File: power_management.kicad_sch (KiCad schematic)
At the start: 36 parts, among them U1 TPS65185

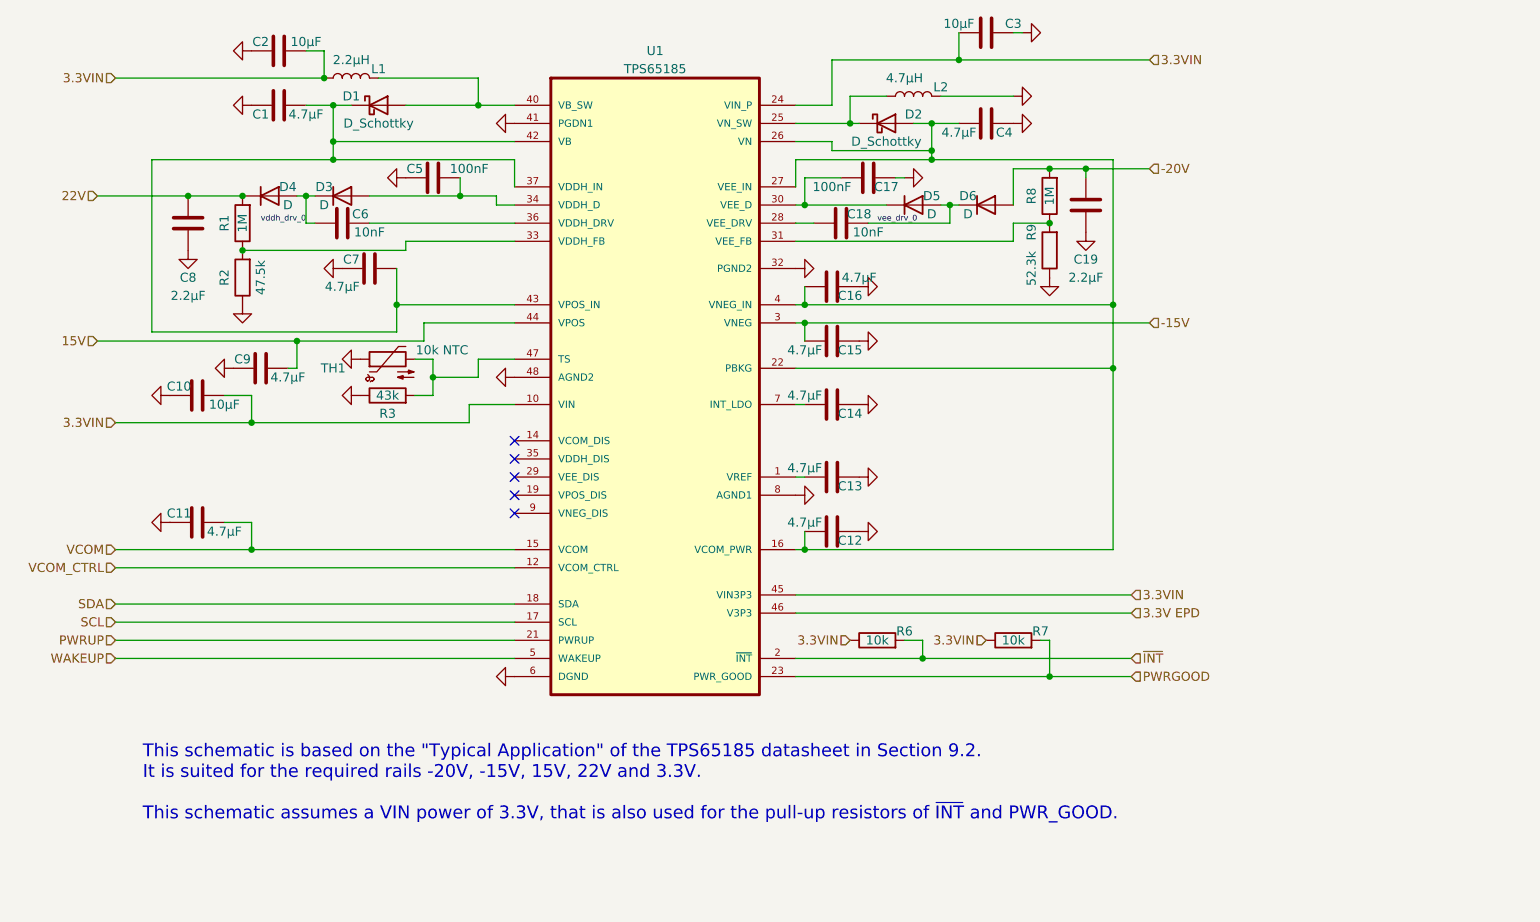
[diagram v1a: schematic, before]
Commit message: Set voltage rating of capacitors
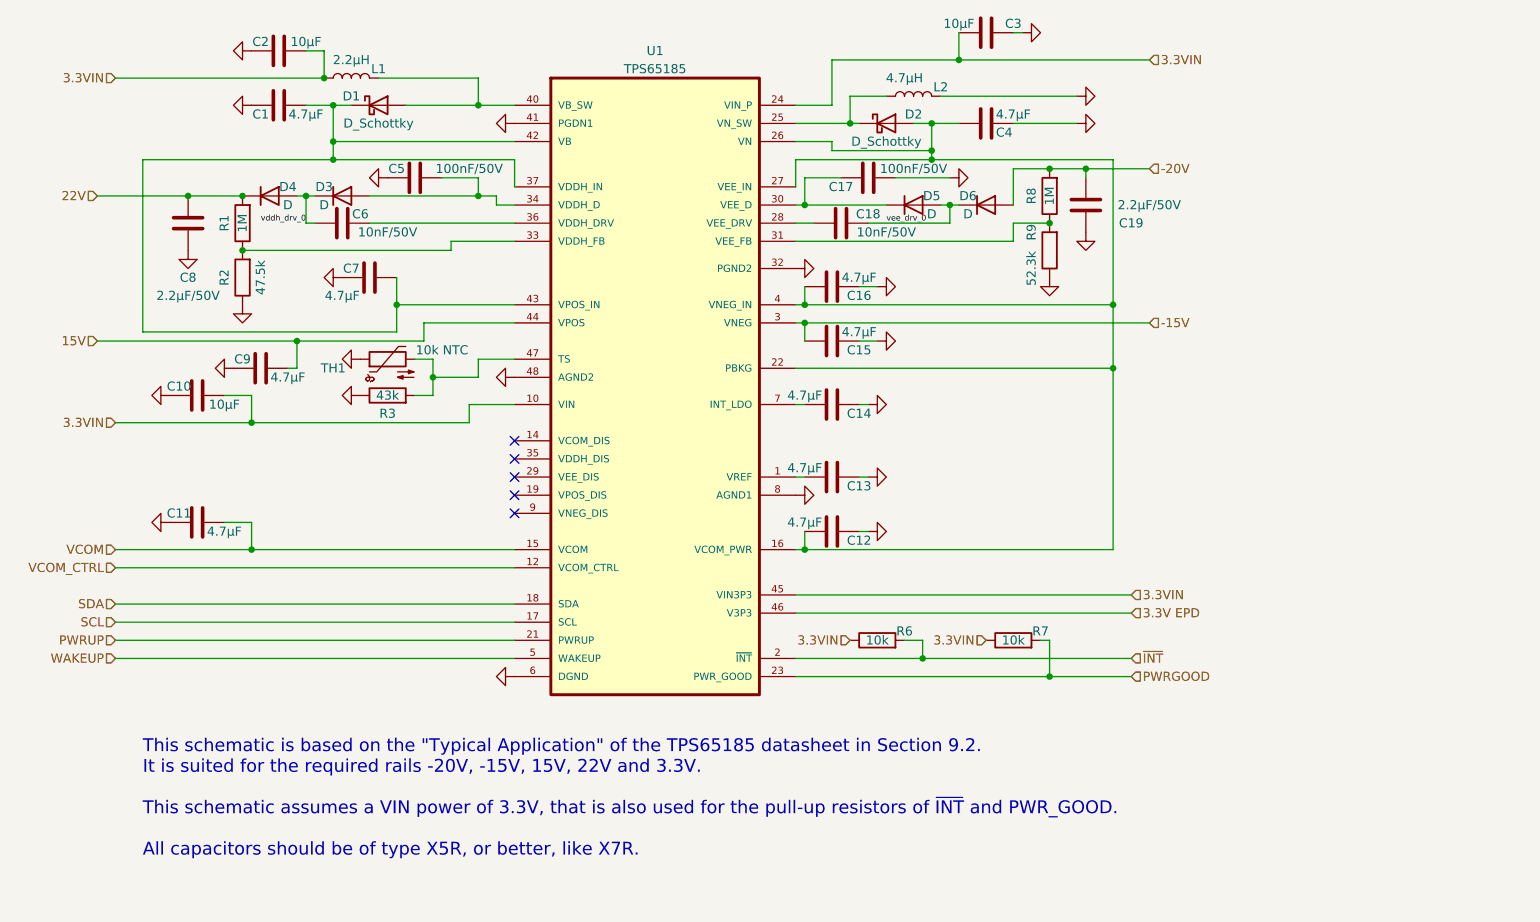
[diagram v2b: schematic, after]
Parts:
- C17, C5: value 100nF -> 100nF/50V
- C18, C6: value 10nF -> 10nF/50V
- C19, C8: value 2.2µF -> 2.2µF/50V
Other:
- note added: "This schematic is based on the "Typical Application" of the TPS65185 datasheet in Section 9.2. It is suited for the required rails -20V, -15V, 15V, 22V and 3.3V. This schematic assumes a VIN power of 3.3V, that is also used for the pull-up resistors of ~{INT} and PWR_GOOD. All capacitors should be of type X5R, or better, like X7R."
- note removed: "This schematic is based on the "Typical Application" of the TPS65185 datasheet in Section 9.2. It is suited for the required rails -20V, -15V, 15V, 22V and 3.3V. This schematic assumes a VIN power of 3.3V, that is also used for the pull-up resistors of ~{INT} and PWR_GOOD."
- moved on the sheet: C5, C7

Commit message: Add footprints and some labels
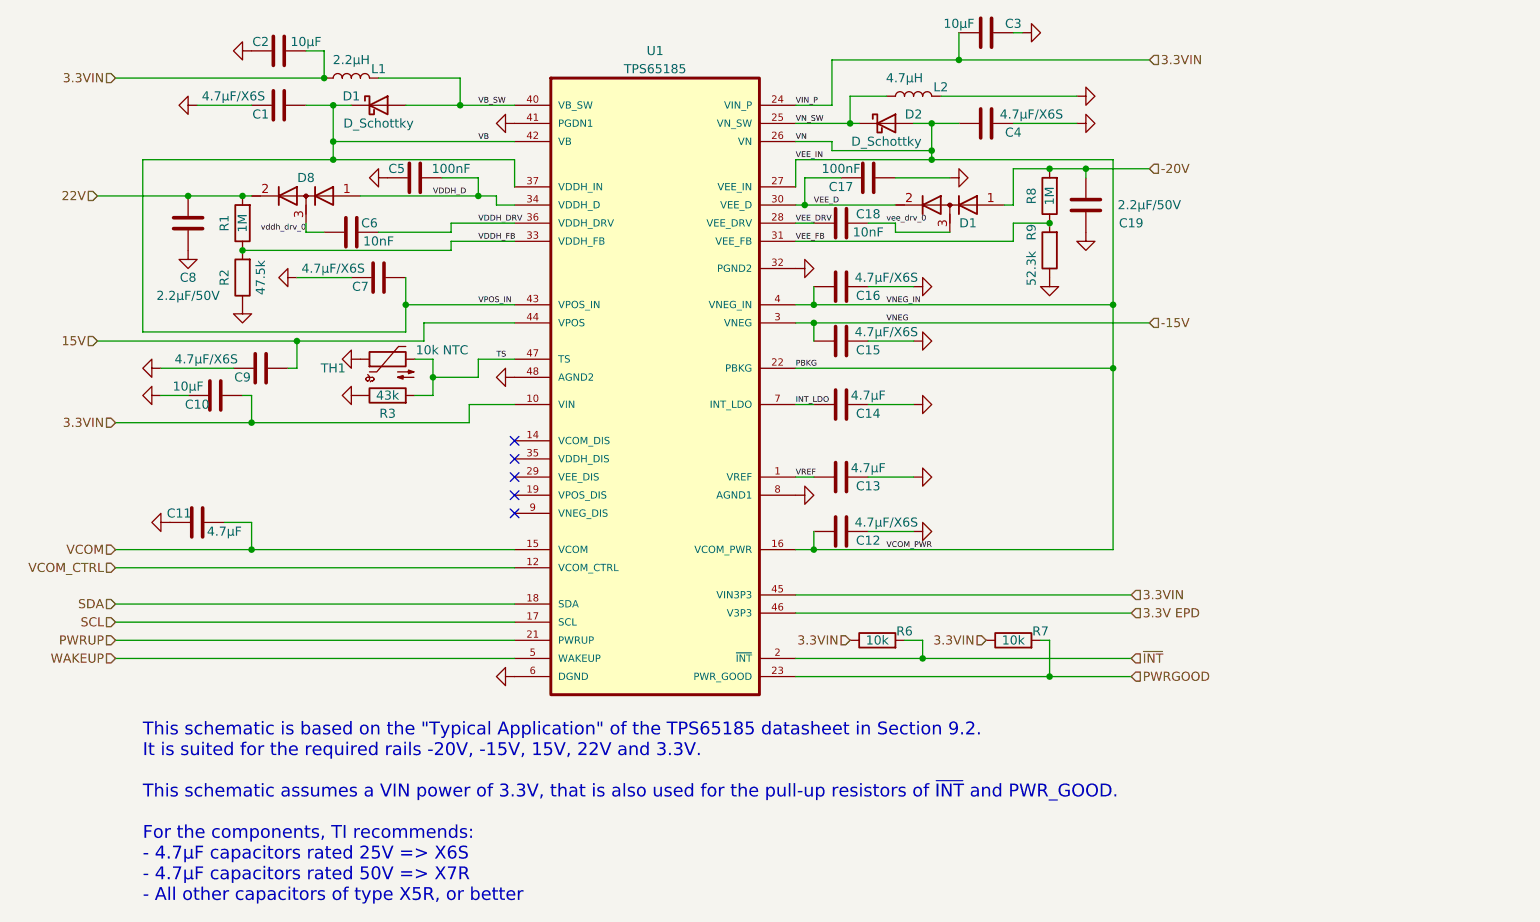
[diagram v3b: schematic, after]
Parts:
- removed D3, D4, D5, D6: D, symbol Device:D
- added D1, D8: D_Dual_Series_AKC, Package_TO_SOT_SMD:SOT-23, symbol Device:D_Dual_Series_AKC
- C1, C12, C15, C16, C4, C7, C9: value 4.7µF -> 4.7µF/X6S; footprint (none) -> Capacitor_SMD:C_0805_2012Metric
- C10, C2, C3: footprint (none) -> Capacitor_SMD:C_0603_1608Metric
- C11, C13, C14, C19, C8: footprint (none) -> Capacitor_SMD:C_0805_2012Metric
- C17, C5: value 100nF/50V -> 100nF; footprint (none) -> Capacitor_SMD:C_0603_1608Metric
- C18, C6: value 10nF/50V -> 10nF; footprint (none) -> Capacitor_SMD:C_0603_1608Metric
- D1, D2: footprint (none) -> Diode_SMD:D_SOD-123
- L1: footprint (none) -> local_lib:TDK_VLS252015ET-2R2M
- L2: footprint (none) -> Inductor_SMD:L_Taiyo-Yuden_NR-40xx
- R1, R2, R3, R6, R7, R8, R9, TH1: footprint (none) -> Resistor_SMD:R_0603_1608Metric
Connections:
- net -20V: now also D1.1 (A)
- net 22V: now also D8.2 (K)
- net vddh_drv_0: now also D8.3 (common)
- net vee_drv_0: now also D1.3 (common)
- net VEE_D: now reaches C17.2, U1.30 (VEE_D)
- net VEE_D: now also D1.2 (K)
- net VDDH_D: now reaches C5.2, U1.34 (VDDH_D)
- net VDDH_D: now also D8.1 (A)
- net INT_LDO: now reaches C14.1, U1.7 (INT_LDO)
- net VN_SW: now reaches D2.1 (K), L2.2, U1.25 (VN_SW)
- net PBKG: now reaches C12.1, C16.1, C4.2, D2.2 (A), U1.16 (VCOM_PWR), U1.22 (PBKG), U1.26 (VN), U1.27 (VEE_IN), U1.4 (VNEG_IN)
- net VDDH_FB: now reaches R1.1, R2.2, U1.33 (VDDH_FB)
- net TS: now reaches R3.2, TH1.2, U1.47 (TS)
- net VB: now reaches C1.2, C7.2, D1.1 (K), U1.37 (VDDH_IN), U1.42 (VB), U1.43 (VPOS_IN)
- net VB_SW: now reaches D1.2 (A), L1.2, U1.40 (VB_SW)
- net VREF: now reaches C13.1, U1.1 (VREF)
- net VEE_FB: now reaches R8.1, R9.2, U1.31 (VEE_FB)
- net VEE_DRV: now reaches C18.1, U1.28 (VEE_DRV)
- net VDDH_DRV: now reaches C6.2, U1.36 (VDDH_DRV)
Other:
- note added: "This schematic is based on the "Typical Application" of the TPS65185 datasheet in Section 9.2. It is suited for the required rails -20V, -15V, 15V, 22V and 3.3V. This schematic assumes a VIN power of 3.3V, that is also used for the pull-up resistors of ~{INT} and PWR_GOOD. For the components, TI recommends: - 4.7µF capacitors rated 25V => X6S - 4.7µF capacitors rated 50V => X7R - All other capaci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"
- note removed: "This schematic is based on the "Typical Application" of the TPS65185 datasheet in Section 9.2. It is suited for the required rails -20V, -15V, 15V, 22V and 3.3V. This schematic assumes a VIN power of 3.3V, that is also used for the pull-up resistors of ~{INT} and PWR_GOOD. All capacitors should be of type X5R, or better, like X7R."
- moved on the sheet: C10, C12, C13, C14, C15, C16, C6, C7

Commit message: Update TPS65185 based on evaluation module
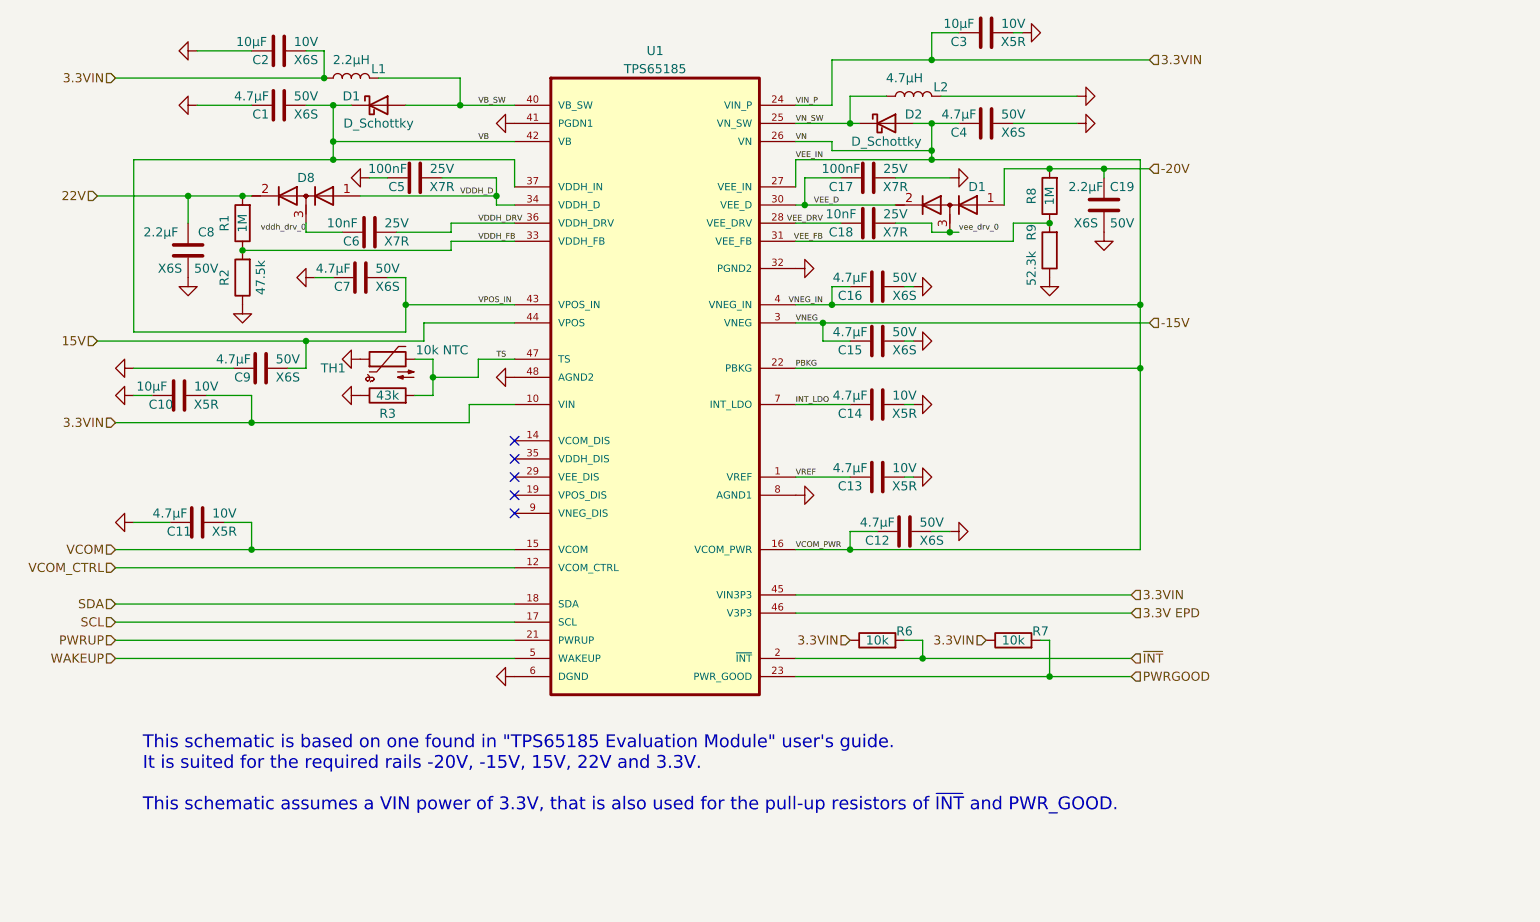
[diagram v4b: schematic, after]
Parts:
- C1, C12, C15, C16, C4, C7, C9: value 4.7µF/X6S -> 4.7µF; Type (none) -> X6S; Voltage (none) -> 50V
- C10, C11, C13, C14, C3: Type (none) -> X5R; Voltage (none) -> 10V
- C17, C18, C5, C6: Type (none) -> X7R; Voltage (none) -> 25V
- C19, C8: value 2.2µF/50V -> 2.2µF; Type (none) -> X6S; Voltage (none) -> 50V
- C2: Type (none) -> X6S; Voltage (none) -> 10V
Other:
- note added: "This schematic is based on one found in "TPS65185 Evaluation Module" user's guide. It is suited for the required rails -20V, -15V, 15V, 22V and 3.3V. This schematic assumes a VIN power of 3.3V, that is also used for the pull-up resistors of ~{INT} and PWR_GOOD."
- note removed: "This schematic is based on the "Typical Application" of the TPS65185 datasheet in Section 9.2. It is suited for the required rails -20V, -15V, 15V, 22V and 3.3V. This schematic assumes a VIN power of 3.3V, that is also used for the pull-up resistors of ~{INT} and PWR_GOOD. For the components, TI recommends: - 4.7µF capacitors rated 25V => X6S - 4.7µF capacitors rated 50V => X7R - All other capaci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"
- moved on the sheet: C10, C12, C13, C14, C15, C16, C18, C19, C6, C7, C8

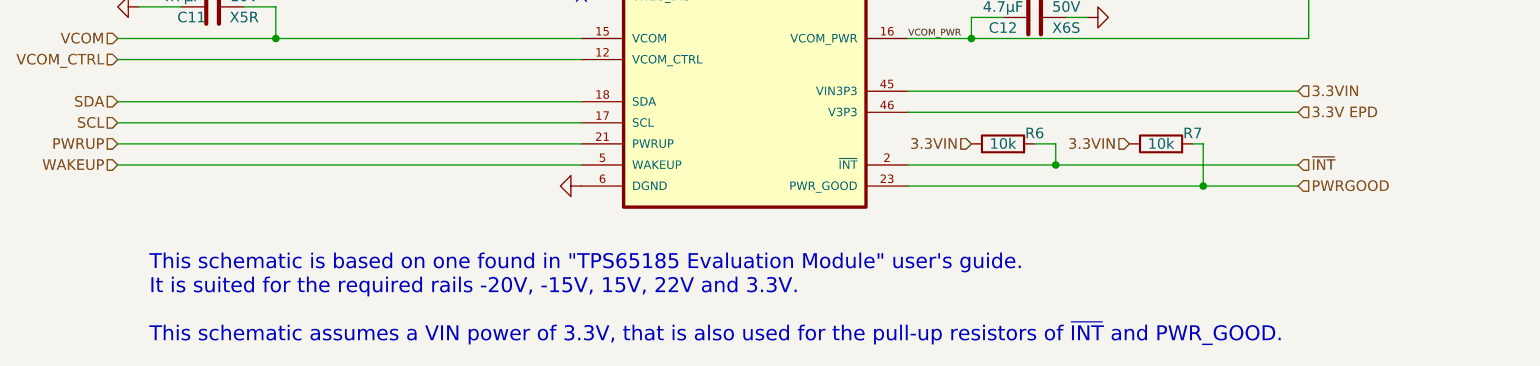
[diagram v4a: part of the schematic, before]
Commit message: Update EPD capacitors
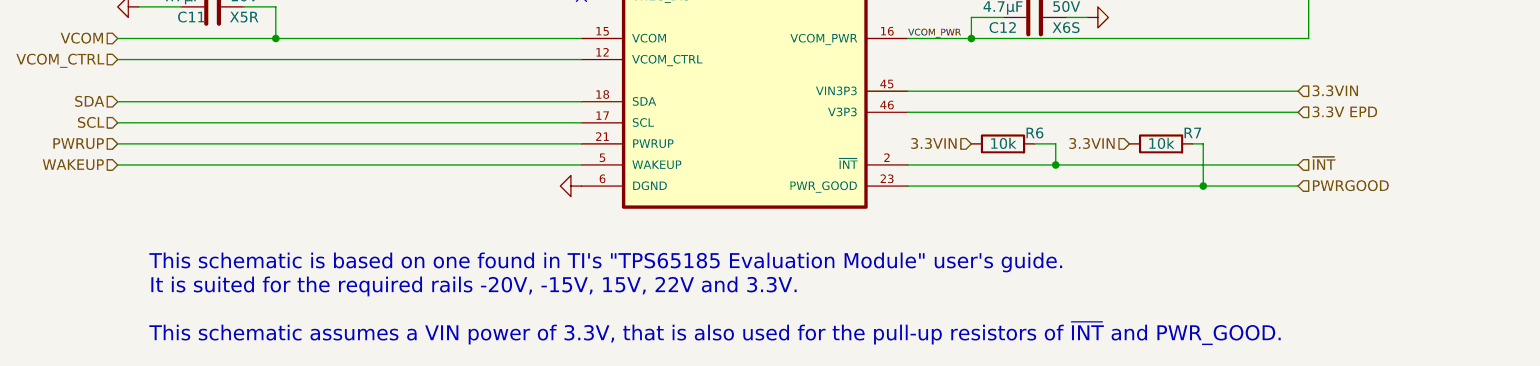
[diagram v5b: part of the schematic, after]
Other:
- note added: "This schematic is based on one found in TI's "TPS65185 Evaluation Module" user's guide. It is suited for the required rails -20V, -15V, 15V, 22V and 3.3V. This schematic assumes a VIN power of 3.3V, that is also used for the pull-up resistors of ~{INT} and PWR_GOOD."
- note removed: "This schematic is based on one found in "TPS65185 Evaluation Module" user's guide. It is suited for the required rails -20V, -15V, 15V, 22V and 3.3V. This schematic assumes a VIN power of 3.3V, that is also used for the pull-up resistors of ~{INT} and PWR_GOOD."
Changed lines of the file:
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@@
     (stroke (width 0) (type default))
   )
-  (text "This schematic is based on one found in \"TPS65185 Evaluation Module\" user's guide.\nIt is suited for the required rails -20V, -15V, 15V, 22V and 3.3V.\n\nThis schematic assumes a VIN power of 3.3V, that is also used for the pull-up resistors of ~{INT} and PWR_GOOD."
+  (text "This schematic is based on one found in TI's \"TPS65185 Evaluation Module\" user's guide.\nIt is suited for the required rails -20V, -15V, 15V, 22V and 3.3V.\n\nThis schematic assumes a VIN power of 3.3V, that is also used for the pull-up resistors of ~{INT} and PWR_GOOD."
     (at 77.47 148.59 0)
     (effects (font (size 1.8 1.8)) (justify left bottom))
